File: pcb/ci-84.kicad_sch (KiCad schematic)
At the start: 24 parts, among them J1 Conn_01x02, SW1 SW_Push, U1 STM32L471RGTx, U2 CR2013-MI2120, U3 TPS63900

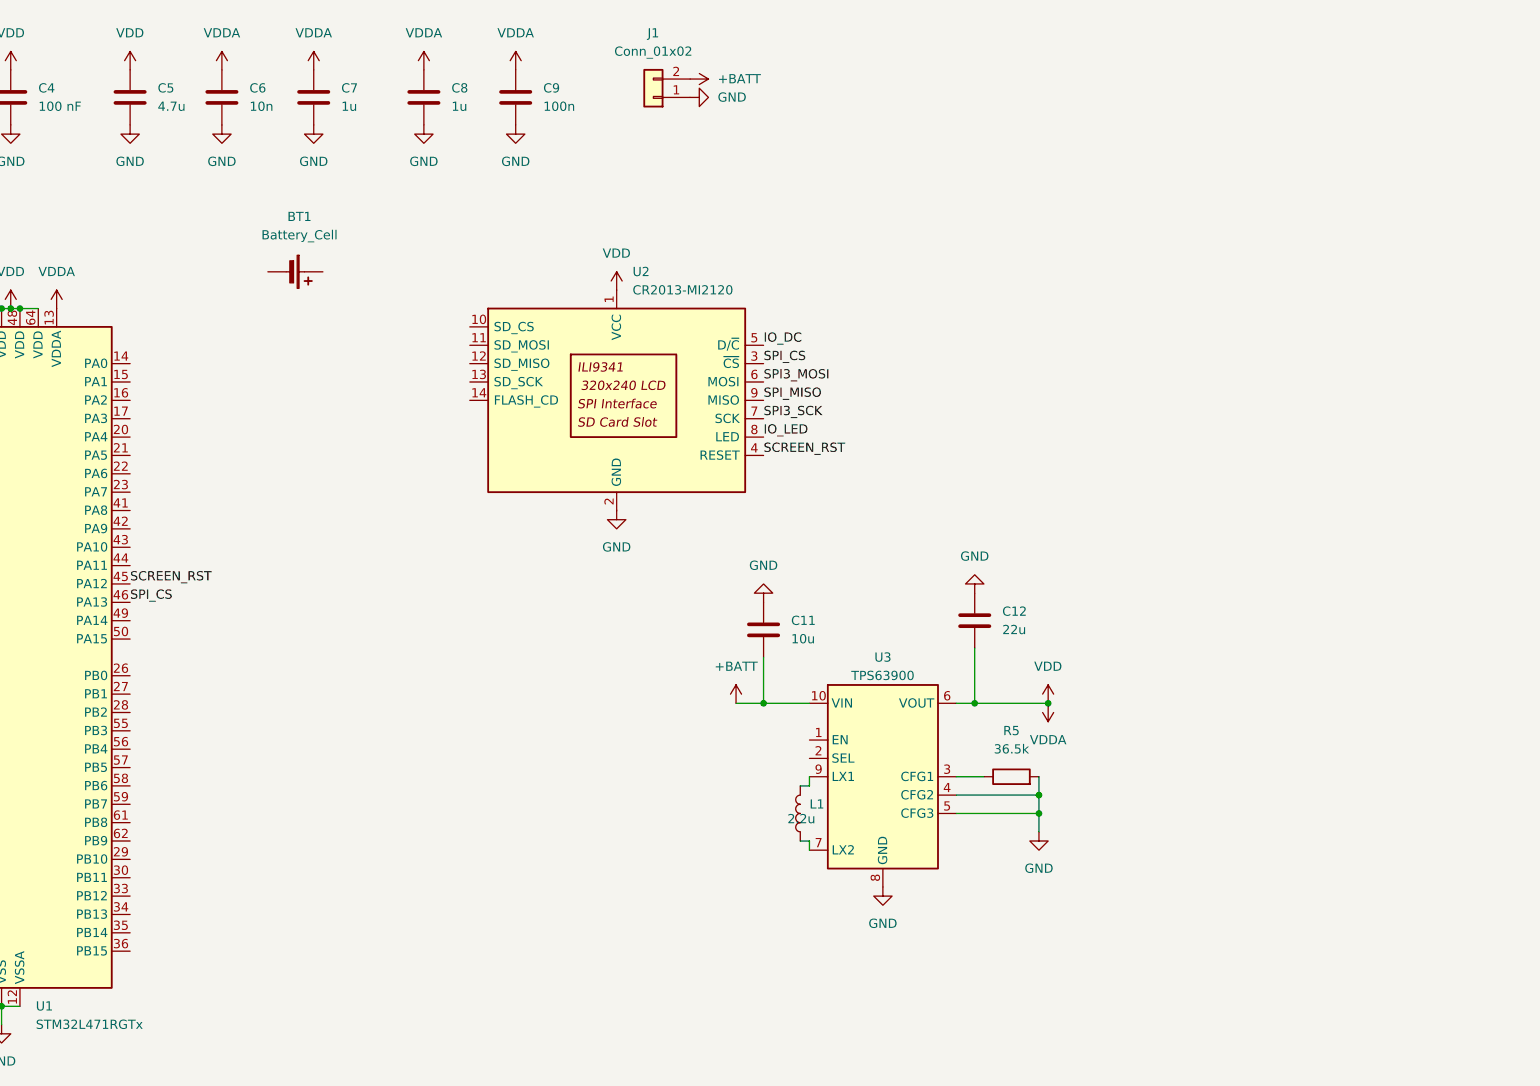
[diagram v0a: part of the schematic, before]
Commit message: keyboard matrix
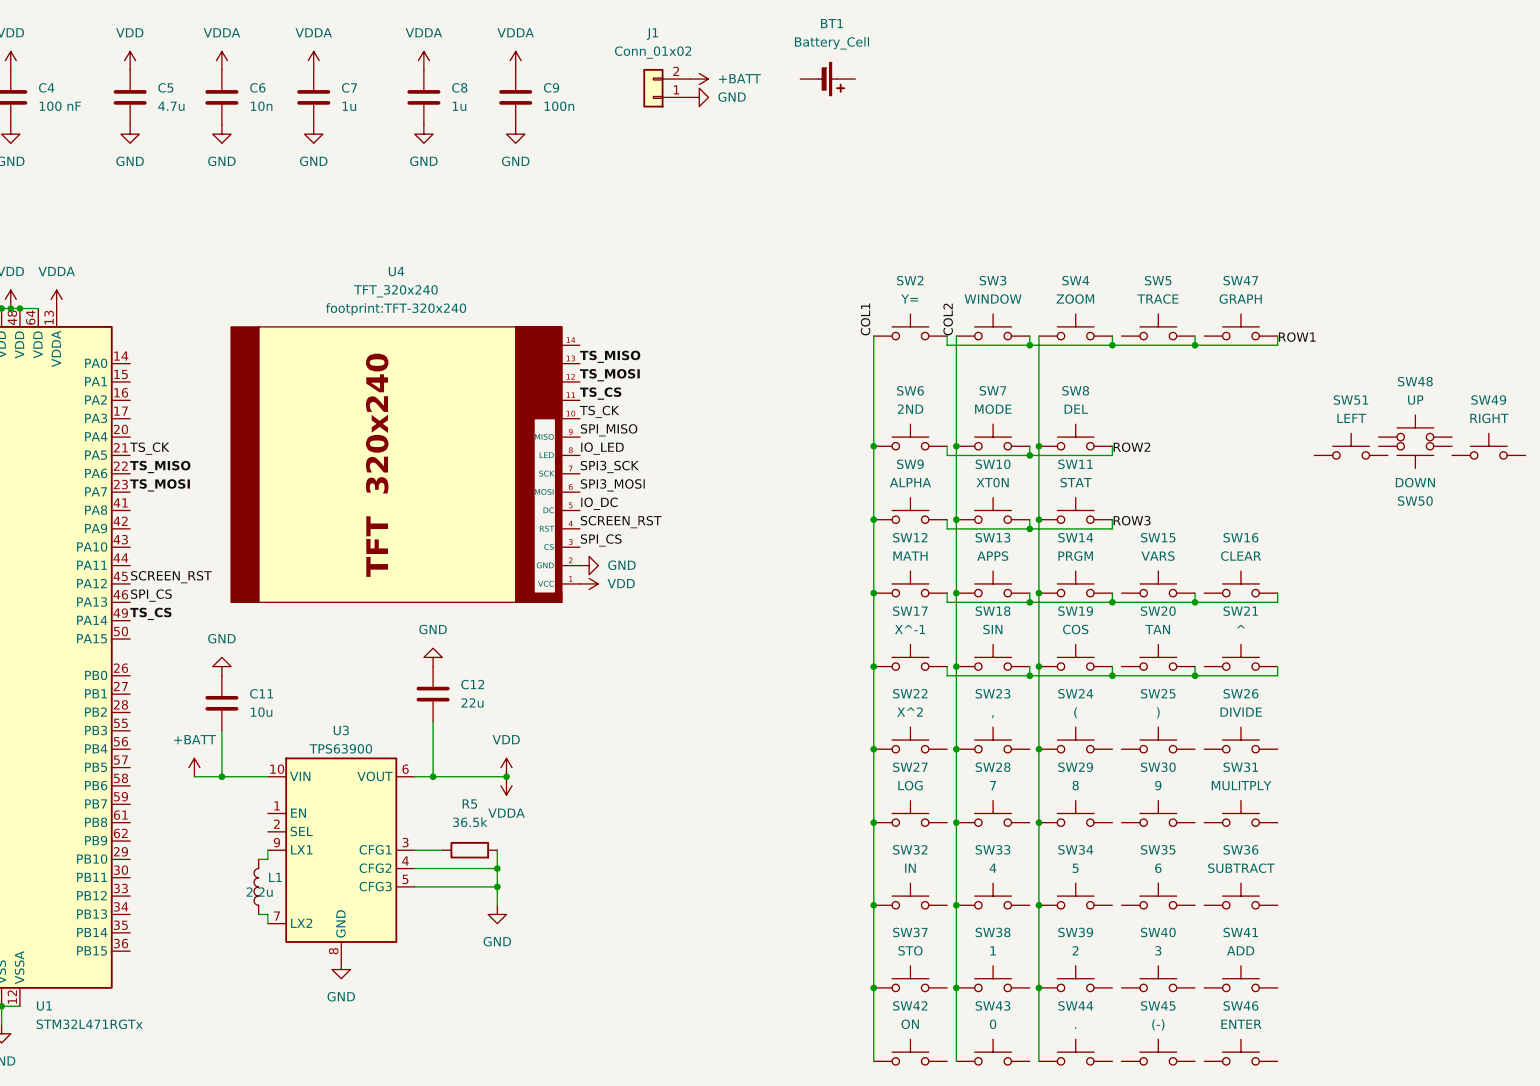
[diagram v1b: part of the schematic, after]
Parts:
- removed U2: CR2013-MI2120, Display:CR2013-MI2120, symbol Driver_Display:CR2013-MI2120
- added SW10: XT0N, symbol Switch:SW_Push
- added SW11: STAT, symbol Switch:SW_Push
- added SW12: MATH, symbol Switch:SW_Push
- added SW13: APPS, symbol Switch:SW_Push
- added SW14: PRGM, symbol Switch:SW_Push
- added SW15: VARS, symbol Switch:SW_Push
- added SW16: CLEAR, symbol Switch:SW_Push
- added SW17: X^-1, symbol Switch:SW_Push
- added SW18: SIN, symbol Switch:SW_Push
- added SW19: COS, symbol Switch:SW_Push
- added SW2: Y=, symbol Switch:SW_Push
- added SW20: TAN, symbol Switch:SW_Push
- added SW21: ^, symbol Switch:SW_Push
- added SW22: X^2, symbol Switch:SW_Push
- added SW23: ,, symbol Switch:SW_Push
- added SW24: (, symbol Switch:SW_Push
- added SW25: ), symbol Switch:SW_Push
- added SW26: DIVIDE, symbol Switch:SW_Push
- added SW27: LOG, symbol Switch:SW_Push
- added SW28: 7, symbol Switch:SW_Push
- added SW29: 8, symbol Switch:SW_Push
- added SW3: WINDOW, symbol Switch:SW_Push
- added SW30: 9, symbol Switch:SW_Push
- added SW31: MULITPLY, symbol Switch:SW_Push
- added SW32: IN, symbol Switch:SW_Push
- added SW33: 4, symbol Switch:SW_Push
- added SW34: 5, symbol Switch:SW_Push
- added SW35: 6, symbol Switch:SW_Push
- added SW36: SUBTRACT, symbol Switch:SW_Push
- added SW37: STO, symbol Switch:SW_Push
- added SW38: 1, symbol Switch:SW_Push
- added SW39: 2, symbol Switch:SW_Push
- added SW4: ZOOM, symbol Switch:SW_Push
- added SW40: 3, symbol Switch:SW_Push
- added SW41: ADD, symbol Switch:SW_Push
- added SW42: ON, symbol Switch:SW_Push
- added SW43: 0, symbol Switch:SW_Push
- added SW44: ., symbol Switch:SW_Push
- added SW45: (-), symbol Switch:SW_Push
- added SW46: ENTER, symbol Switch:SW_Push
- added SW47: GRAPH, symbol Switch:SW_Push
- added SW48: UP, symbol Switch:SW_Push
- added SW49: RIGHT, symbol Switch:SW_Push
- added SW5: TRACE, symbol Switch:SW_Push
- added SW50: DOWN, symbol Switch:SW_Push
- added SW51: LEFT, symbol Switch:SW_Push
- added SW6: 2ND, symbol Switch:SW_Push
- added SW7: MODE, symbol Switch:SW_Push
- added SW8: DEL, symbol Switch:SW_Push
- added SW9: ALPHA, symbol Switch:SW_Push
- added U4: TFT_320x240, footprint:TFT-320x240, symbol tft_320x240:TFT_320x240
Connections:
- net GND: now also U4.2 (GND)
- net IO_DC: now also U4.5 (DC)
- net IO_LED: now also U4.8 (LED)
- net SCREEN_RST: now also U4.4 (RST)
- net SPI3_MOSI: now also U4.6 (MOSI)
- net SPI3_SCK: now also U4.7 (SCK)
- net SPI_CS: now also U4.3 (CS)
- net SPI_MISO: now also U4.9 (MISO)
- net VDD: now also U4.1 (VCC)
- net TS_CK: now reaches U1.21 (PA5)
- net TS_CK: now also U4.10
- net TS_MISO: now reaches U1.22 (PA6)
- net TS_MISO: now also U4.13
- net TS_MOSI: now reaches U1.23 (PA7)
- net TS_MOSI: now also U4.12
- net TS_CS: now reaches U1.49 (PA14)
- net TS_CS: now also U4.11
- new net: SW17.1, SW18.1, SW19.1, SW20.1, SW21.1
- new net: SW12.1, SW13.1, SW14.1, SW15.1, SW16.1
- new net: SW11.2, SW14.2, SW19.2, SW24.2, SW29.2, SW34.2, SW39.2, SW4.2, SW44.2, SW8.2
- new net COL1: SW12.2, SW17.2, SW2.1, SW22.2, SW27.2, SW32.2, SW37.2, SW42.2, SW6.2, SW9.2
- new net COL2: SW10.2, SW13.2, SW18.2, SW23.2, SW28.2, SW3.2, SW33.2, SW38.2, SW43.2, SW7.2
- new net ROW1: SW2.2, SW3.1, SW4.1, SW47.1, SW5.1
- new net ROW2: SW6.1, SW7.1, SW8.1
- new net ROW3: SW10.1, SW11.1, SW9.1
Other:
- note added: "T_CLK"
- note added: "T_CS"
- note added: "T_DIN"
- note added: "T_DO"
- note added: "T_IRQ"
- moved on the sheet: BT1, C11, C12, L1, R5, U3

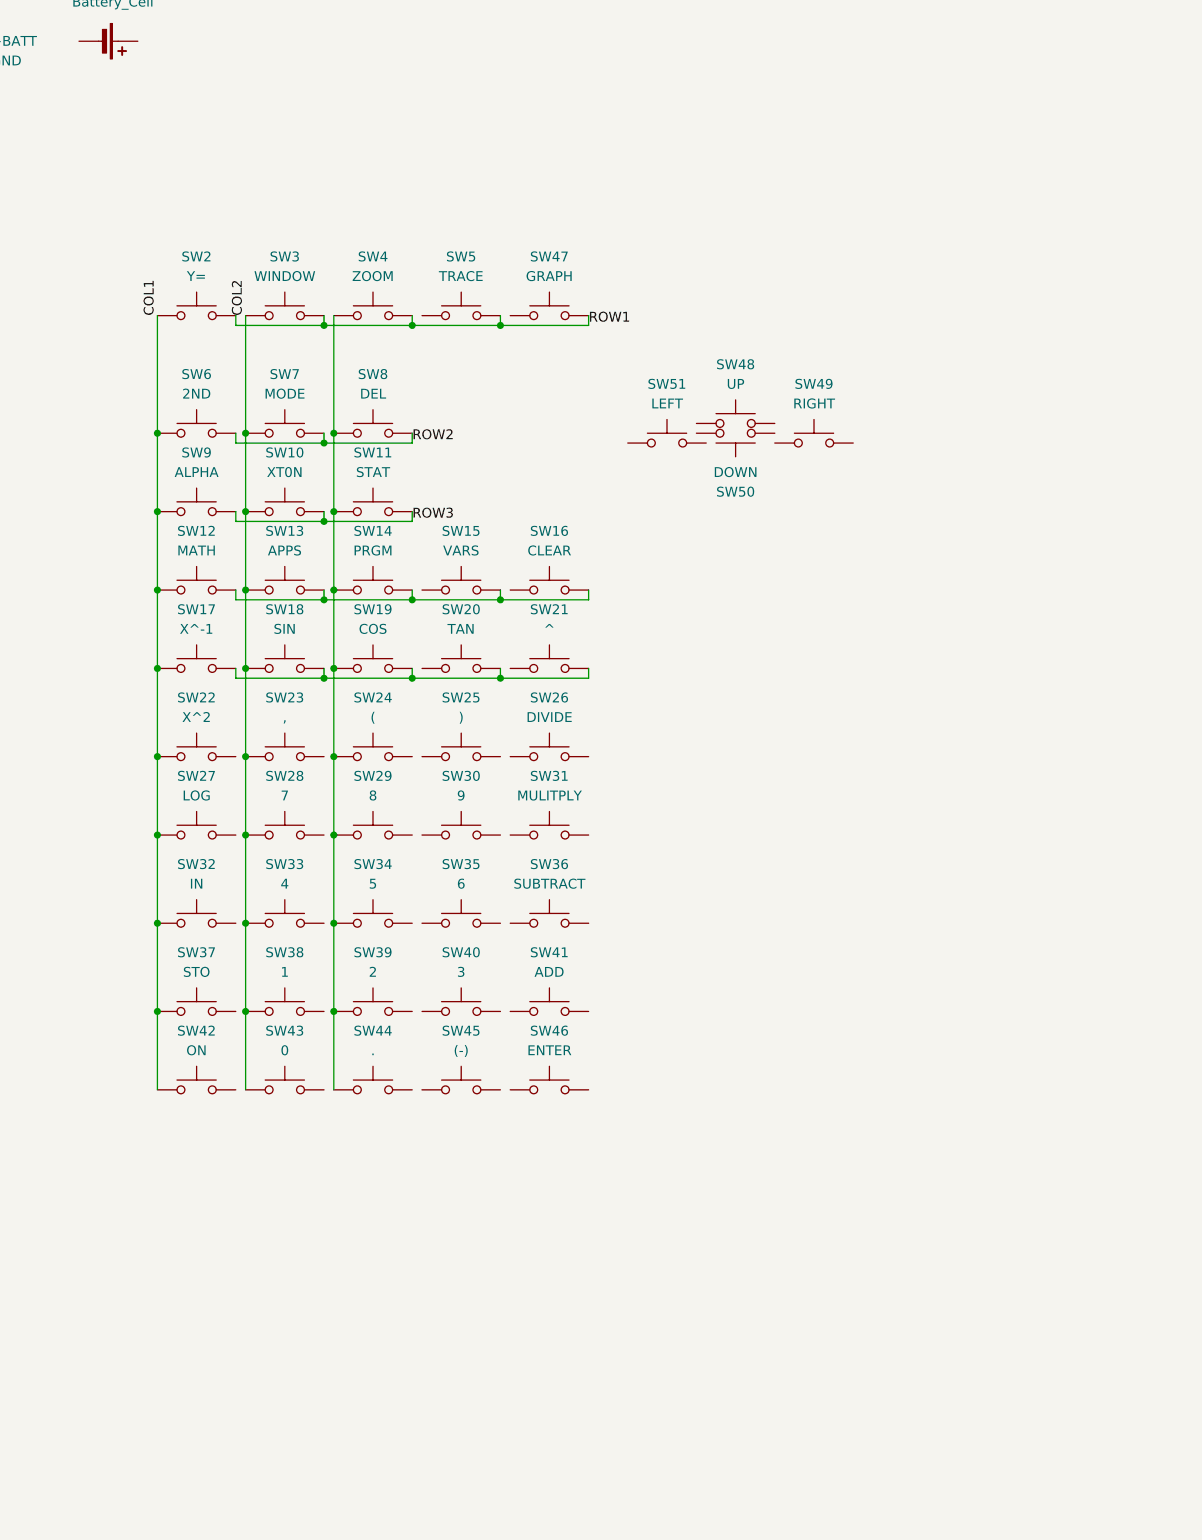
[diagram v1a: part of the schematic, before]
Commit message: add diode matrix, start
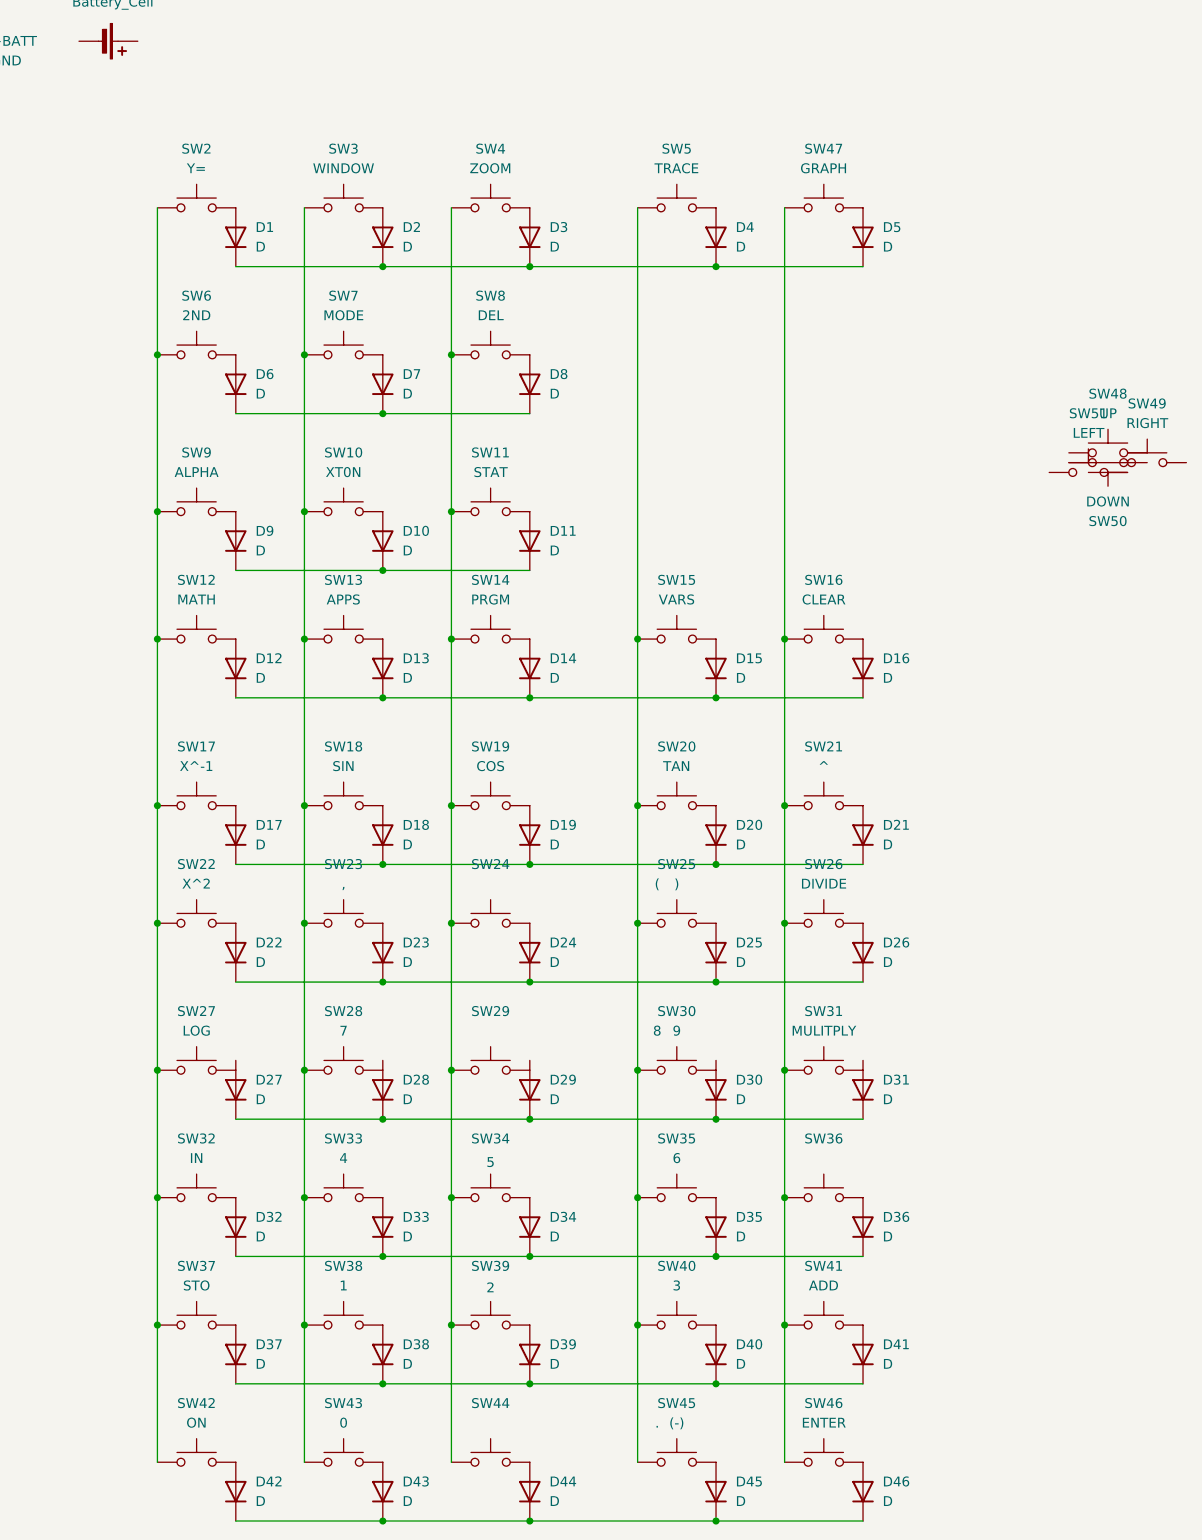
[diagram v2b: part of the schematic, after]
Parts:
- added D1, D10, D11, D12, D13, D14, D15, D16, D17, D18, D19, D2, D20, D21, D22, D23, D24, D25, D26, D27, D28, D29, D3, D30, D31, D32, D33, D34, D35, D36, D37, D38, D39, D4, D40, D41, D42, D43, D44, D45, D46, D5, D6, D7, D8, D9: D, Diode_SMD:D_SOD-123, symbol Device:D
- SW10, SW11, SW12, SW13, SW14, SW15, SW16, SW17, SW18, SW19, SW2, SW20, SW21, SW22, SW23, SW24, SW25, SW26, SW27, SW28, SW29, SW3, SW30, SW31, SW32, SW33, SW34, SW35, SW36, SW37, SW38, SW39, SW4, SW40, SW41, SW42, SW43, SW44, SW45, SW46, SW47, SW48, SW49, SW5, SW50, SW51, SW6, SW7, SW8, SW9: footprint (none) -> Button_Switch_SMD:SW_Tactile_SPST_NO_Straight_CK_PTS636Sx25SMTRLFS
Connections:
- net at SW46.1: now also D46.2 (A)
- net at SW46.2: now also SW16.2, SW21.2, SW26.2, SW31.2, SW36.2, SW41.2, SW47.2
- net at SW26.1: now also D26.2 (A)
- net at SW30.2: now also SW15.2, SW20.2, SW25.2, SW35.2, SW40.2, SW45.2, SW5.2
- net at SW36.1: now also D36.2 (A)
- net at SW33.1: now also D33.2 (A)
- net at SW39.1: now also D39.2 (A)
- net at SW23.1: now also D23.2 (A)
- net at SW35.1: now also D35.2 (A)
- net at SW38.1: now also D38.2 (A)
- net at SW25.1: now also D25.2 (A)
- net at SW24.1: now also D24.2 (A)
- net at SW42.1: now also D42.2 (A)
- net at SW41.1: now also D41.2 (A)
- net at SW32.1: now also D32.2 (A)
- net at SW37.1: now also D37.2 (A)
- net at SW43.1: now also D43.2 (A)
- net at SW34.1: now also D34.2 (A)
- net at SW45.1: now also D45.2 (A)
- net at SW40.1: now also D40.2 (A)
- net at SW44.1: now also D44.2 (A)
- net at SW22.1: now also D22.2 (A)
- net COL1: no longer names the net of SW12.2, SW17.2, SW2.1, SW22.2, SW27.2, SW32.2, SW37.2, SW42.2, SW6.2, SW9.2
- net COL2: no longer names the net of SW10.2, SW13.2, SW18.2, SW23.2, SW28.2, SW3.2, SW33.2, SW38.2, SW43.2, SW7.2
- removed net ROW1: SW2.2, SW3.1, SW4.1, SW47.1, SW5.1
- removed net ROW2: SW6.1, SW7.1, SW8.1
- removed net ROW3: SW10.1, SW11.1, SW9.1
- new net: D12.1 (K), D13.1 (K), D14.1 (K), D15.1 (K), D16.1 (K)
- new net: D16.2 (A), SW16.1
- new net: D42.1 (K), D43.1 (K), D44.1 (K), D45.1 (K), D46.1 (K)
- new net: D37.1 (K), D38.1 (K), D39.1 (K), D40.1 (K), D41.1 (K)
- new net: D17.1 (K), D18.1 (K), D19.1 (K), D20.1 (K), D21.1 (K)
- new net: D21.2 (A), SW21.1
- new net: D18.2 (A), SW18.1
- new net: D17.2 (A), SW17.1
- new net: D14.2 (A), SW14.1
- new net: D1.2 (A), SW2.2
- new net: D22.1 (K), D23.1 (K), D24.1 (K), D25.1 (K), D26.1 (K)
- new net: D10.2 (A), SW10.1
- new net: D10.1 (K), D11.1 (K), D9.1 (K)
- new net: D8.2 (A), SW8.1
- new net: D11.2 (A), SW11.1
- new net: D7.2 (A), SW7.1
- new net: D6.1 (K), D7.1 (K), D8.1 (K)
- new net: D27.1 (K), D28.1 (K), D29.1 (K), D30.1 (K), D31.1 (K)
- new net: D15.2 (A), SW15.1
- new net: D32.1 (K), D33.1 (K), D34.1 (K), D35.1 (K), D36.1 (K)
- new net: D13.2 (A), SW13.1
- new net: D3.2 (A), SW4.1
- new net: D5.2 (A), SW47.1
- new net: D1.1 (K), D2.1 (K), D3.1 (K), D4.1 (K), D5.1 (K)
- new net: D9.2 (A), SW9.1
- new net: D19.2 (A), SW19.1
- new net: D12.2 (A), SW12.1
- new net: D4.2 (A), SW5.1
- new net: D2.2 (A), SW3.1
- new net: D6.2 (A), SW6.1
- new net: D20.2 (A), SW20.1
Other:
- moved on the sheet: SW10, SW11, SW12, SW13, SW14, SW15, SW16, SW17, SW18, SW19, SW2, SW20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
